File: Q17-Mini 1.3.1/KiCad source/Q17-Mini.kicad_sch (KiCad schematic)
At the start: 86 parts, among them J1 INPUT, J2-1 SPK+, J2-2 SPK-, J3-1 V+, J3-2 GND, J3-3 V-, Q1 IRF610, Q10 KSA992, Q11 ZVP2106A, Q12 BD139, Q13 IRF610, Q14 IRF9610, Q15 FQA46N15, Q16 FQA36P15, Q2 KSA992, Q3 KSC1845, Q4 IRF9610, Q5 FQP3P20, Q6 FQP3N30, Q7 KSC1845, Q8 ZVN4206AV, Q9 ZVP2106A, U1 OPA1611

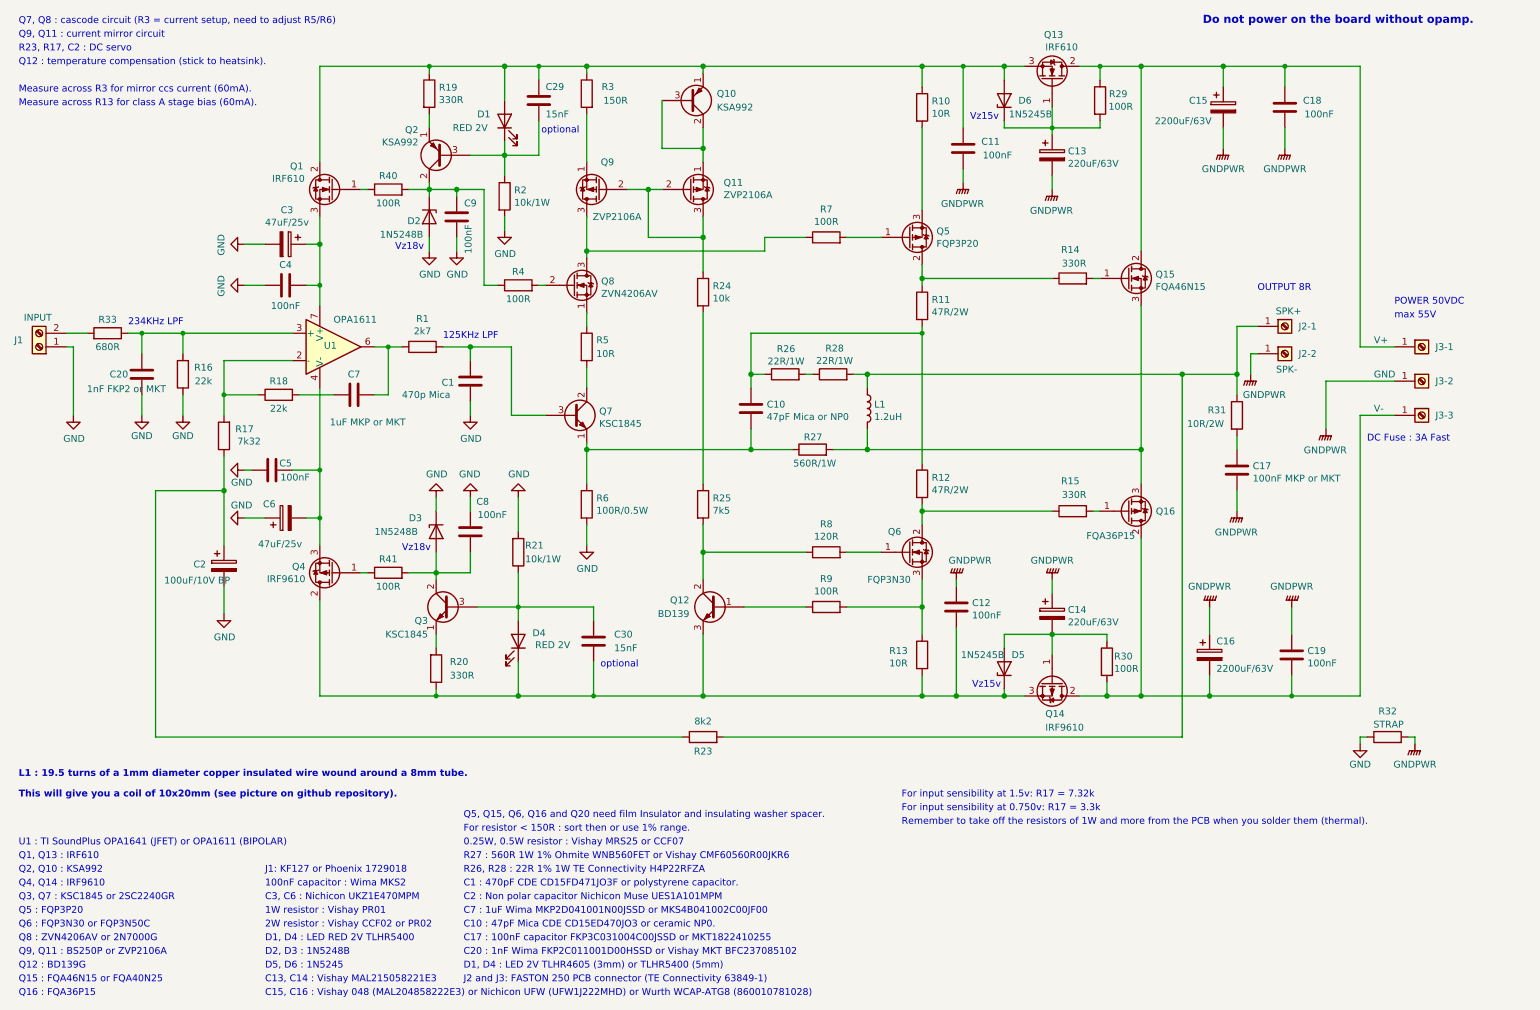
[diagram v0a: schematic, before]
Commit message: Updated Q17-Mini to version 1.3.1
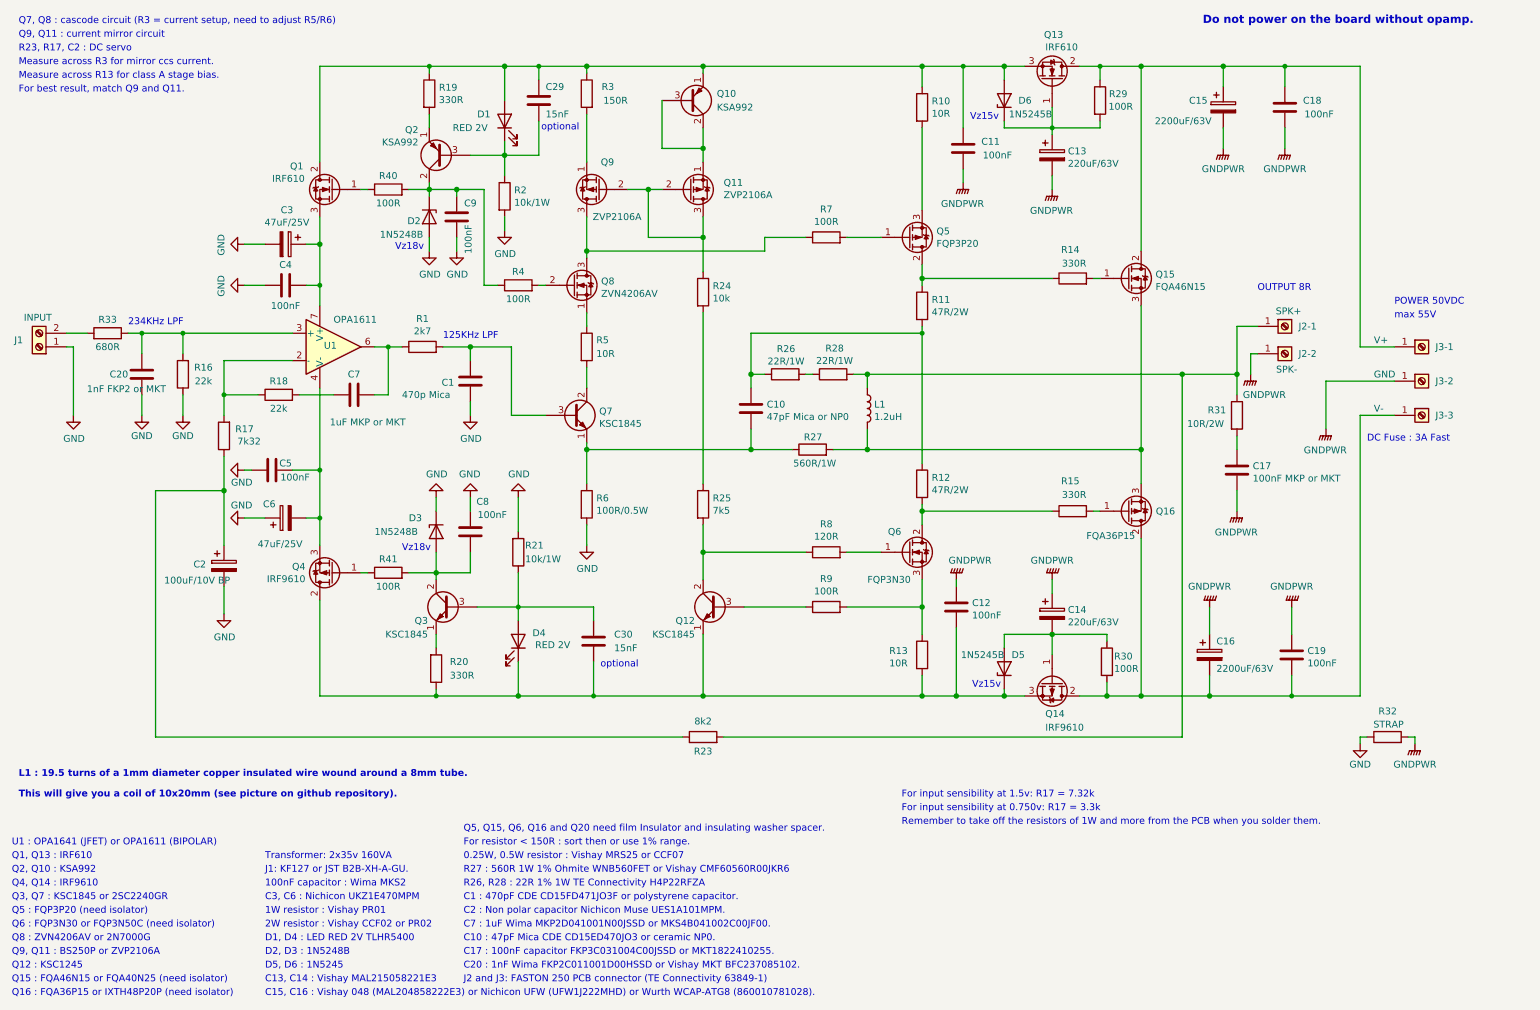
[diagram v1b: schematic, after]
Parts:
- removed Q12: BD139, Q17_Library:Q12_BD139, symbol Device:Q_NPN_BCE
- added Q12: KSC1845, Package_TO_SOT_THT:TO-92_Inline_Wide, symbol Device:Q_NPN_ECB
- C3, C6: value 47uF/25v -> 47uF/25V
- J1: footprint TerminalBlock_Phoenix:TerminalBlock_Phoenix_PT-1,5-2-5.0-H_1x02_P5.00mm_Horizontal -> Q17_Library:Input_connector_mix_inverted
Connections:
- net at C12.2, C30.2, D4.1 (K)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: now also Q12.1 (E)
- net at R9.1: now also Q12.3 (B)
- net at R25.2, R8.1: now also Q12.2 (C)
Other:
- note added: "C15, C16 : Vishay 048 (MAL204858222E3) or Nichicon UFW (UFW1J222MHD) or Wurth WCAP-ATG8 (860010781028)."
- note added: "C17 : 100nF capacitor FKP3C031004C00JSSD or MKT1822410255."
- note added: "C2 : Non polar capacitor Nichicon Muse UES1A101MPM."
- note added: "C20 : 1nF Wima FKP2C011001D00HSSD or Vishay MKT BFC237085102."
- note added: "C7 : 1uF Wima MKP2D041001N00JSSD or MKS4B041002C00JF00."
- note added: "For best result, match Q9 and Q11."
- note added: "J1: KF127 or JST B2B-XH-A-GU."
- note added: "Measure across R13 for class A stage bias."
- note added: "Measure across R3 for mirror ccs current."
- note added: "Q12 : KSC1245"
- note added: "Q15 : FQA46N15 or FQA40N25 (need isolator)"
- note added: "Q16 : FQA36P15 or IXTH48P20P (need isolator)"
- note added: "Q5 : FQP3P20 (need isolator)"
- note added: "Q6 : FQP3N30 or FQP3N50C (need isolator)"
- note added: "Remember to take off the resistors of 1W and more from the PCB when you solder them."
- note added: "Transformer: 2x35v 160VA"
- note added: "U1 : OPA1641 (JFET) or OPA1611 (BIPOLAR)"
- note removed: "C15, C16 : Vishay 048 (MAL204858222E3) or Nichicon UFW (UFW1J222MHD) or Wurth WCAP-ATG8 (860010781028)"
- note removed: "C17 : 100nF capacitor FKP3C031004C00JSSD or MKT1822410255"
- note removed: "C2 : Non polar capacitor Nichicon Muse UES1A101MPM"
- note removed: "C20 : 1nF Wima FKP2C011001D00HSSD or Vishay MKT BFC237085102"
- note removed: "C7 : 1uF Wima MKP2D041001N00JSSD or MKS4B041002C00JF00"
- note removed: "D1, D4 : LED 2V TLHR4605 (3mm) or TLHR5400 (5mm)"
- note removed: "J1: KF127 or Phoenix 1729018"
- note removed: "Measure across R13 for class A stage bias (60mA)."
- note removed: "Measure across R3 for mirror ccs current (60mA)."
- note removed: "Q12 : BD139G"
- note removed: "Q12 : temperature compensation (stick to heatsink)."
- note removed: "Q15 : FQA46N15 or FQA40N25"
- note removed: "Q16 : FQA36P15"
- note removed: "Q5 : FQP3P20"
- note removed: "Q6 : FQP3N30 or FQP3N50C"
- note removed: "Remember to take off the resistors of 1W and more from the PCB when you solder them (thermal)."
- note removed: "U1 : TI SoundPlus OPA1641 (JFET) or OPA1611 (BIPOLAR)"
